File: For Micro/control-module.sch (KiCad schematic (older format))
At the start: 23 parts, among them J1 For Light Sensor, J2 For Light Sensor, J3 From Solar Panel, J4 For Flow Module b, J5 For Flow Module a, U1 STR05, U2 ARDUINO_MICRO_SHIELD

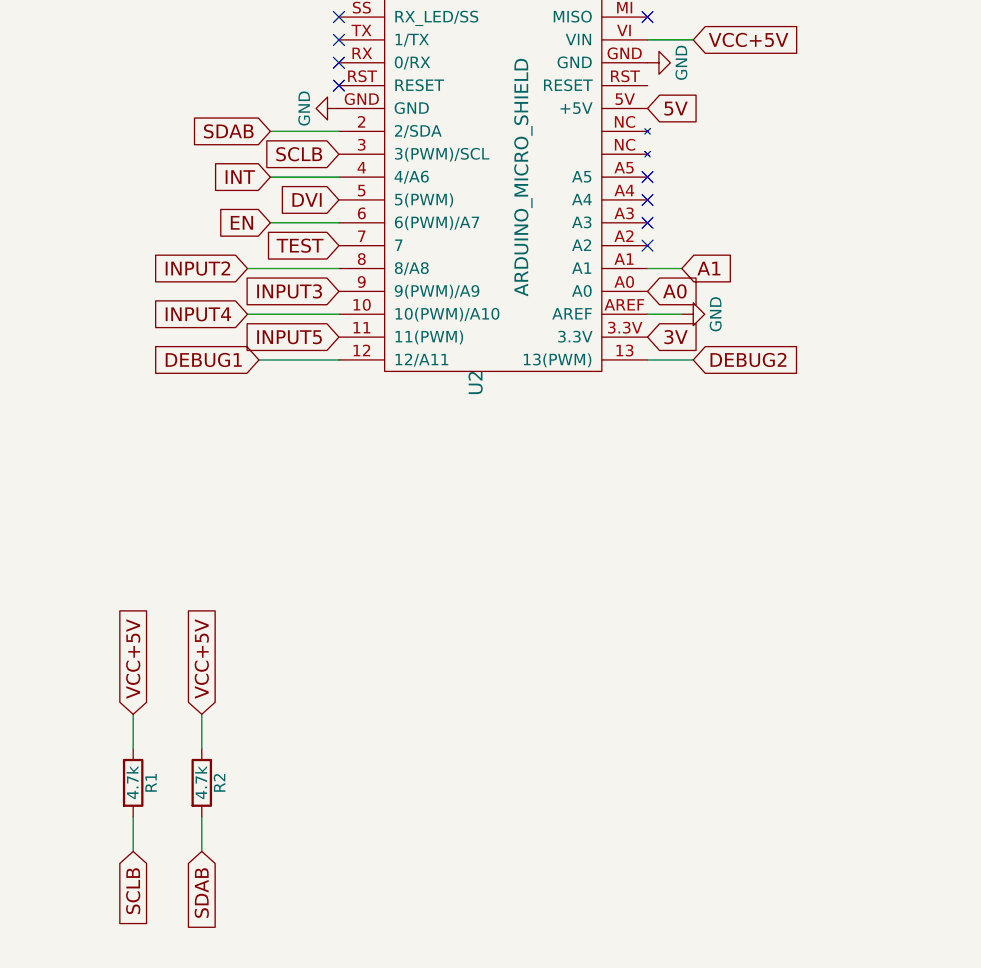
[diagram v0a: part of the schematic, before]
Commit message: Cleaned up control code, verified at this point. Added NMOS to Control CAD
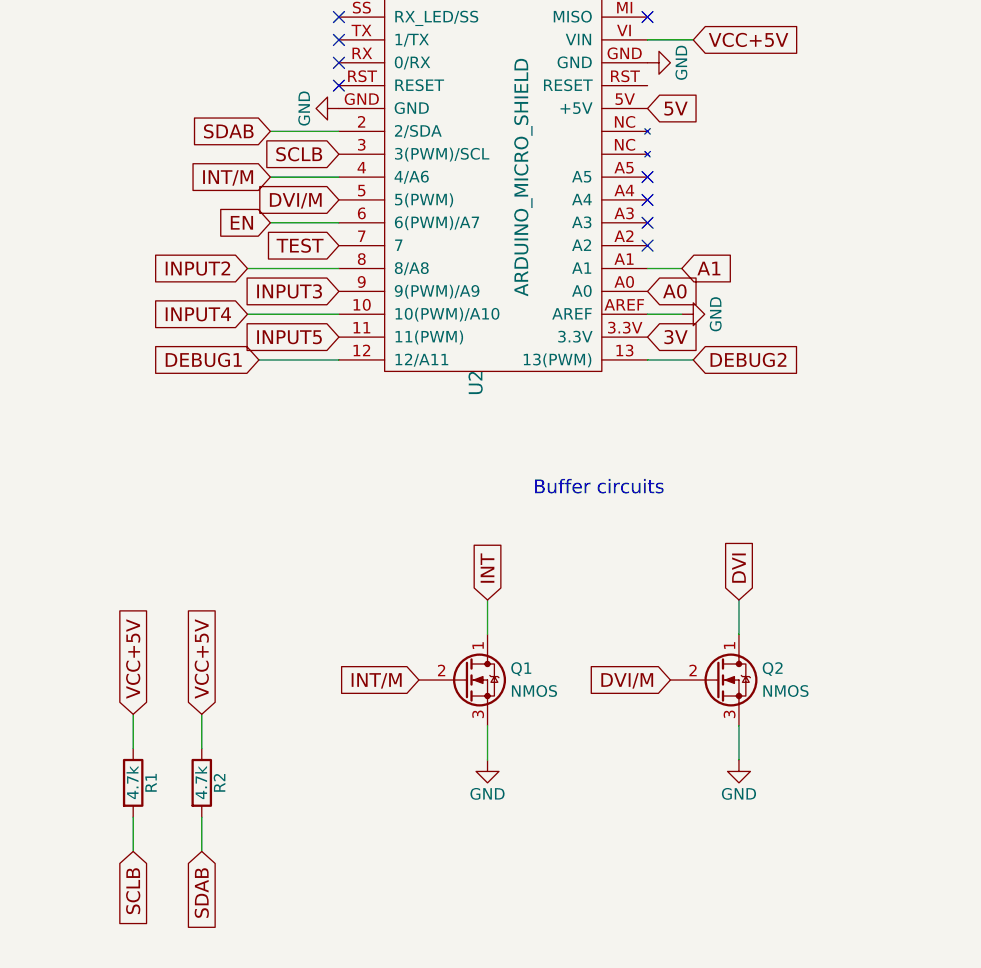
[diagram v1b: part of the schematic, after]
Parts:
- added Q1, Q2: NMOS, TO_SOT_Packages_SMD:SOT-23_Handsoldering, symbol Q_NMOS_DGS
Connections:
- net DVI: now also Q2.1 (D); no longer U2.5 (5(PWM))
- net GND: now also Q1.3 (S), Q2.3 (S)
- net INT: now also Q1.1 (D); no longer U2.4 (4/A6)
- new net DVI/M: Q2.2 (G), U2.5 (5(PWM))
- new net INT/M: Q1.2 (G), U2.4 (4/A6)
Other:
- note added: "Buffer circuits\n"
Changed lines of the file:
@@
 Text GLabel 7750 3450 2    60   Input ~ 0
 DEBUG2
-Text GLabel 5900 2650 0    60   Input ~ 0
-INT
-Text GLabel 6200 2750 0    60   Input ~ 0
-DVI
 Text GLabel 5900 2450 0    60   Input ~ 0
 SDAB
@@
 NoConn ~ 7550 2850
 NoConn ~ 7550 2950
+$Comp
+L Q_NMOS_DGS Q1
+U 1 1 5B0C07DB
+P 6750 4850
+F 0 "Q1" H 6950 4900 50  0000 L CNN
+F 1 "NMOS" H 6950 4800 50  0000 L CNN
+F 2 "TO_SOT_Packages_SMD:SOT-23_Handsoldering" H 6950 4950 50  0001 C CNN
+F 3 "" H 6750 4850 50  0001 C CNN
+	1    6750 4850
+	1    0    0    -1
+$EndComp
+Text GLabel 5900 2650 0    60   Input ~ 0
+INT/M
+Text GLabel 6550 4850 0    60   Input ~ 0
+INT/M
+Text GLabel 6200 2750 0    60   Input ~ 0
+DVI/M
+Text GLabel 6850 4500 1    60   Input ~ 0
+INT
+$Comp
+L GND #PWR020
+U 1 1 5B0C1583
+P 6850 5200
+F 0 "#PWR020" H 6850 4950 50  0001 C CNN
+F 1 "GND" H 6850 5050 50  0000 C CNN
+F 2 "" H 6850 5200 50  0001 C CNN
+F 3 "" H 6850 5200 50  0001 C CNN
+	1    6850 5200
+	1    0    0    -1
+$EndComp
+$Comp
+L Q_NMOS_DGS Q2
+U 1 1 5B0C16A2
+P 7850 4850
+F 0 "Q2" H 8050 4900 50  0000 L CNN
+F 1 "NMOS" H 8050 4800 50  0000 L CNN
+F 2 "TO_SOT_Packages_SMD:SOT-23_Handsoldering" H 8050 4950 50  0001 C CNN
+F 3 "" H 7850 4850 50  0001 C CNN
+	1    7850 4850
+	1    0    0    -1
+$EndComp
+Text GLabel 7650 4850 0    60   Input ~ 0
+DVI/M
+Text GLabel 7950 4500 1    60   Input ~ 0
+DVI
+$Comp
+L GND #PWR021
+U 1 1 5B0C1811
+P 7950 5200
+F 0 "#PWR021" H 7950 4950 50  0001 C CNN
+F 1 "GND" H 7950 5050 50  0000 C CNN
+F 2 "" H 7950 5200 50  0001 C CNN
+F 3 "" H 7950 5200 50  0001 C CNN
+	1    7950 5200
+	1    0    0    -1
+$EndComp
 Wire Wire Line
 	3800 1450 3800 1350
@@
 Wire Wire Line
 	6200 2450 5900 2450
+Wire Wire Line
+	6850 4500 6850 4650
+Wire Wire Line
+	7950 4500 7950 4650
+Wire Wire Line
+	7950 5050 7950 5200
+Wire Wire Line
+	6850 5200 6850 5050
+Text Notes 7050 4050 0    60   ~ 0
+Buffer circuits\n
 $EndSCHEMATC

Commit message: Add MOSFET circuits, power LED, regulator, connector and jumpers
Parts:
- removed C1, C2, C3: 4.7uF, Capacitors_SMD:C_0805_HandSoldering, symbol C_Small
- removed L1: 3.3uH, valveteam-footprints:WURTH_INDUCTOR, symbol L
- removed U1: STR05, valveteam-footprints:STR05, symbol STR05
- added C1, C2, C3, C4: 10uF, symbol C
- added D4: LED, LEDs:LED_0805_HandSoldering, symbol LED-RESCUE-control-module
- added J4: To Flow Module (F), valveteam-footprints:TE_TERM, symbol Conn_01x02
- added JP1, JP2, JP3: Jumper_NO_Small, symbol Jumper_NO_Small
- added L1, L2: 6.8uH, symbol INDUCTOR
- added Q1, Q2: NMOS, TO_SOT_Packages_SMD:SOT-23_Handsoldering, symbol Q_NMOS_DGS
- added R6: 470, Resistors_SMD:R_0805_HandSoldering, symbol R
- added U1, U2: TR_SERIES, symbol TR_SERIES
- D1, D2, D3: symbol LED -> LED-RESCUE-control-module
- R4, R5: value 150 -> 470
- renumbered J4 to J5, J5 to J6, Q1 to Q3, Q2 to Q4, U2 to U3
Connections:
- net 12V: now also D1.2 (A), C1.1, C3.1, J4.1 (Pin_1), L1.1, L2.1; no longer R3.1
- net DVI/M: now also U3.7; no longer U3.5 (5(PWM))
- net GND: now also R3.2, R5.2, C1.2, C2.2, C3.2, C4.2, J4.2 (Pin_2), Q1.3 (S), Q2.3 (S), R6.2, U1.GND, U2.GND; no longer D1.1 (K), D3.1 (K)
- net INT/M: now also U3.6 (6(PWM)/A7); no longer U3.4 (4/A6)
- net TEST: now also U3.5 (5(PWM)); no longer U3.7
- net VCC+3V: now also D4.2 (A), JP2.2, JP3.2, U2.VO; no longer I2Crepeater1.~ (VCC(B)), I2Crepeater2.~ (VCC(B)), J1.1 (Pin_1), J2.1 (Pin_1)
- net VCC+5V: now also D3.2 (A), JP1.2, U1.VO; no longer R5.1
- net EN2/M: now reaches U3.A2
- net EN2/M: now also Q2.2 (G)
- removed net EN: I2Crepeater1.~ (VCC(B)), I2Crepeater2.~ (VCC(B)), U3.6 (6(PWM)/A7)
- new net: D1.1 (K), R3.1
- new net: D3.1 (K), R5.1
- new net: C2.1, L1.2, U1.VI
- new net: C4.1, L2.2, U2.VI
- new net: D4.1 (K), R6.1
- new net EN1: I2Crepeater2.~ (VCC(B)), Q1.1 (D)
- new net EN1/M: Q1.2 (G), U3.4 (4/A6)
- new net EN2: I2Crepeater1.~ (VCC(B)), Q2.1 (D)
- new net VCC+EXP: I2Crepeater1.~ (VCC(B)), J1.1 (Pin_1), JP1.1, JP2.1
- new net VCC+LS: I2Crepeater2.~ (VCC(B)), J2.1 (Pin_1), JP3.1
- no-connect marks 13 -> 12
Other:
- note added: "Arduino Micro (E)"
- note added: "Connectors for Flow Module (A)"
- note added: "I2C Circuits for Light Sensor (F/E)\n"
- note added: "I2C Pullup Resistors"
- note added: "Jumpers To Supply Voltage\nfor Expansion (F)"
- note added: "MOSFET Pull Down Circuits (E)\n"
- note added: "Power Status LEDs (E)"
- note removed: "Buffer circuits\n"
- note removed: "Connectors for Flow Module"
- note removed: "I2C Circuits for Light Sensor\n"
- note removed: "Power Status LEDs"
- moved on the sheet: D1, D2, D3, I2Crepeater1, I2Crepeater2, J1, J2, J5, J6, Q3, Q4, R1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

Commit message: PCB for Control
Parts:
- added RV3: Trimmer Upper, Potentiometers:Potentiometer_Trimmer_Vishay_T73XX_Vertical, symbol POT_TRIM
- C1, C2, C3, C4: footprint (none) -> Capacitors_SMD:C_0805_HandSoldering
- J1: value For Light Sensor -> For Expansion
- JP1, JP2, JP3: footprint (none) -> valveteam-footprints:SMD-solder-bridge
- L1, L2: footprint (none) -> valveteam-footprints:WURTH_INDUCTOR
- U1, U2: footprint (none) -> valveteam-footprints:TR_Series
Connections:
- net 5V: now also RV3.1
- net GND: now also RV3.3
- net A3: now reaches U3.A3
- net A3: now also RV3.2
- net 3V: no longer names the net of U3.3.3V
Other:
- moved on the sheet: RV1, RV2
